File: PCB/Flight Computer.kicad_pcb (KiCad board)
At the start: 6 copper layers, 30 x 60 mm, 115 parts, among them J401 Conn_01x05_Pin, J402 USB_C_Receptacle_USB2.0_16P, J403 Screw_Terminal_01x06, J404 Screw_Terminal_01x04, J405 Conn_02x04_Counter_Clockwise, J406 Conn_02x03_Counter_Clockwise, J407 Conn_01x06_Pin, J408 Conn_01x04, J501 Conn_Coaxial, Q101 FDN306P, Q401 SL2302S, Q601 SL2302S, Q602 SL2302S, Q603 SL2302S, SW401 SW_Push, SW402 SW_Push, U101 LM1117MP-3.3, U201 STM32F446RETx, U202 W25Q128JVS, U301 SAM-M8Q, U302 LSM6DSV320, U303 MMC5633NJL, U304 MS5607-02BA, U501 SX1262IMLTRT, U502 SKY13453-385LF, Y201 Resonator, Y501 32 MHz

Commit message: Used KiCad's annotation tool to reannotate some of the parts Updated BOM
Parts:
- renumbered D406 to D403, D403 to D404, J407 to J403, J403 to J404, J404 to J405, J405 to J406, J406 to J407, R203 to R202, R202 to R203, R404 to R403, R406 to R404, R407 to R405, R408 to R406
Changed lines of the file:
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@@
 		(descr "2.0mm x 2.0mm Addressable RGB LED NeoPixel Nano, 12 mA, https://cdn-shop.adafruit.com/product-files/4684/4684_WS2812B-2020_V1.3_EN.pdf")
 		(tags "LED RGB NeoPixel Nano PLCC-4 2020")
-		(property "Reference" "D403"
+		(property "Reference" "D404"
 			(at 0 -2 0)
 			(layer "User.1")
@@
 		(descr "Through hole straight pin header, 1x06, 2.54mm pitch, single row")
 		(tags "Through hole pin header THT 1x06 2.54mm single row")
-		(property "Reference" "J407"
+		(property "Reference" "J403"
 			(at 0 -2.38 0)
 			(layer "F.Fab")
@@
 			)
 		)
-		(attr through_hole)
+		(attr through_hole exclude_from_pos_files exclude_from_bom)
 		(duplicate_pad_numbers_are_jumpers no)
 		(fp_line
@@
 		(descr "Resistor SMD 0603 (1608 Metric), square (rectangular) end terminal, IPC-7351 nominal with elongated pad for handsoldering. (Body size source: IPC-SM-782 page 72, https://www.pcb-3d.com/wordpress/wp-content/uploads/ipc-sm-782a_amendment_1_and_2.pdf), generated with kicad-footprint-generator")
 		(tags "resistor handsolder")
-		(property "Reference" "R404"
+		(property "Reference" "R403"
 			(at 0 -1.43 90)
 			(layer "User.1")
@@
 		(descr "Terminal Block Phoenix MPT-0,5-4-2.54, 4 pins, pitch 2.54mm, size 10.6x6.2mm, drill diameter 1.1mm, pad diameter 2.2mm, http://www.mouser.com/ds/2/324/ItemDetail_1725672-916605.pdf, script-generated using https://gitlab.com/kicad/libraries/kicad-footprint-generator/-/tree/master/scripts/TerminalBlock_Phoenix")
 		(tags "THT Terminal Block Phoenix MPT-0,5-4-2.54 pitch 2.54mm size 10.6x6.2mm drill 1.1mm pad 2.2mm")
-		(property "Reference" "J404"
+		(property "Reference" "J405"
 			(at -0.000001 1.97 90)
 			(layer "User.1")
@@
 		(layer "F.Cu")
 		(at 125.5 76.63 -90)
-		(property "Reference" "J405"
+		(property "Reference" "J406"
 			(at 2.032 2.54 270)
 			(unlocked yes)
@@
 			)
 		)
-		(attr smd)
+		(attr smd exclude_from_pos_files exclude_from_bom)
 		(duplicate_pad_numbers_are_jumpers no)
 		(fp_rect
@@
 		(descr "Terminal Block Phoenix MPT-0,5-6-2.54, 6 pins, pitch 2.54mm, size 15.7x6.2mm, drill diameter 1.1mm, pad diameter 2.2mm, http://www.mouser.com/ds/2/324/ItemDetail_1725672-916605.pdf, script-generated using https://gitlab.com/kicad/libraries/kicad-footprint-generator/-/tree/master/scripts/TerminalBlock_Phoenix")
 		(tags "THT Terminal Block Phoenix MPT-0,5-6-2.54 pitch 2.54mm size 15.7x6.2mm drill 1.1mm pad 2.2mm")
-		(property "Reference" "J403"
+		(property "Reference" "J404"
 			(at 0 2.05 90)
 			(layer "User.1")
@@
 		(descr "LED SMD 0603 (1608 Metric), square (rectangular) end terminal, IPC-7351 nominal, (Body size source: http://www.tortai-tech.com/upload/download/2011102023233369053.pdf), generated with kicad-footprint-generator")
 		(tags "LED handsolder")
-		(property "Reference" "D406"
+		(property "Reference" "D403"
 			(at 0 -1.43 90)
 			(layer "User.1")
@@
 			)
 		)
-		(attr through_hole)
+		(attr through_hole exclude_from_pos_files exclude_from_bom)
 		(duplicate_pad_numbers_are_jumpers no)
 		(fp_line
@@
 		(layer "F.Cu")
 		(at 115.47 54.35)
-		(property "Reference" "J406"
+		(property "Reference" "J407"
 			(at -1.17 0.006 90)
 			(unlocked yes)
@@
 			)
 		)
-		(attr smd exclude_from_bom)
+		(attr smd exclude_from_pos_files exclude_from_bom)
 		(duplicate_pad_numbers_are_jumpers no)
 		(fp_rect
@@
 		(descr "Resistor SMD 0603 (1608 Metric), square (rectangular) end terminal, IPC-7351 nominal with elongated pad for handsoldering. (Body size source: IPC-SM-782 page 72, https://www.pcb-3d.com/wordpress/wp-content/uploads/ipc-sm-782a_amendment_1_and_2.pdf), generated with kicad-footprint-generator")
 		(tags "resistor handsolder")
-		(property "Reference" "R406"
+		(property "Reference" "R404"
 			(at 0 1.43 90)
 			(layer "User.1")
@@
 		(descr "Resistor SMD 0603 (1608 Metric), square (rectangular) end terminal, IPC-7351 nominal with elongated pad for handsoldering. (Body size source: IPC-SM-782 page 72, https://www.pcb-3d.com/wordpress/wp-content/uploads/ipc-sm-782a_amendment_1_and_2.pdf), generated with kicad-footprint-generator")
 		(tags "resistor handsolder")
-		(property "Reference" "R407"
+		(property "Reference" "R405"
 			(at 0 1.43 0)
 			(layer "User.2")
@@
 		(descr "Resistor SMD 0603 (1608 Metric), square (rectangular) end terminal, IPC-7351 nominal with elongated pad for handsoldering. (Body size source: IPC-SM-782 page 72, https://www.pcb-3d.com/wordpress/wp-content/uploads/ipc-sm-782a_amendment_1_and_2.pdf), generated with kicad-footprint-generator")
 		(tags "resistor handsolder")
-		(property "Reference" "R202"
+		(property "Reference" "R203"
 			(at 0 1.43 0)
 			(layer "User.2")
@@
 		(descr "Resistor SMD 0603 (1608 Metric), square (rectangular) end terminal, IPC-7351 nominal with elongated pad for handsoldering. (Body size source: IPC-SM-782 page 72, https://www.pcb-3d.com/wordpress/wp-content/uploads/ipc-sm-782a_amendment_1_and_2.pdf), generated with kicad-footprint-generator")
 		(tags "resistor handsolder")
-		(property "Reference" "R408"
+		(property "Reference" "R406"
 			(at 0 1.43 90)
 			(layer "User.2")
@@
 		(descr "Resistor SMD 0603 (1608 Metric), square (rectangular) end terminal, IPC-7351 nominal with elongated pad for handsoldering. (Body size source: IPC-SM-782 page 72, https://www.pcb-3d.com/wordpress/wp-content/uploads/ipc-sm-782a_amendment_1_and_2.pdf), generated with kicad-footprint-generator")
 		(tags "resistor handsolder")
-		(property "Reference" "R203"
+		(property "Reference" "R202"
 			(at 0 1.43 90)
 			(layer "User.2")

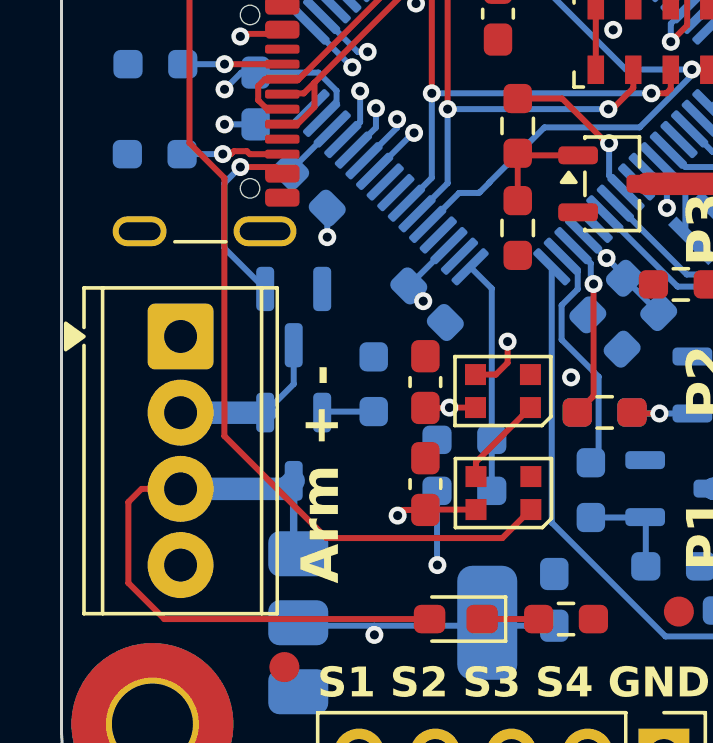
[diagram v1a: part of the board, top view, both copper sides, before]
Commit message: Made it so USB isn't putting 4.7v into the battery
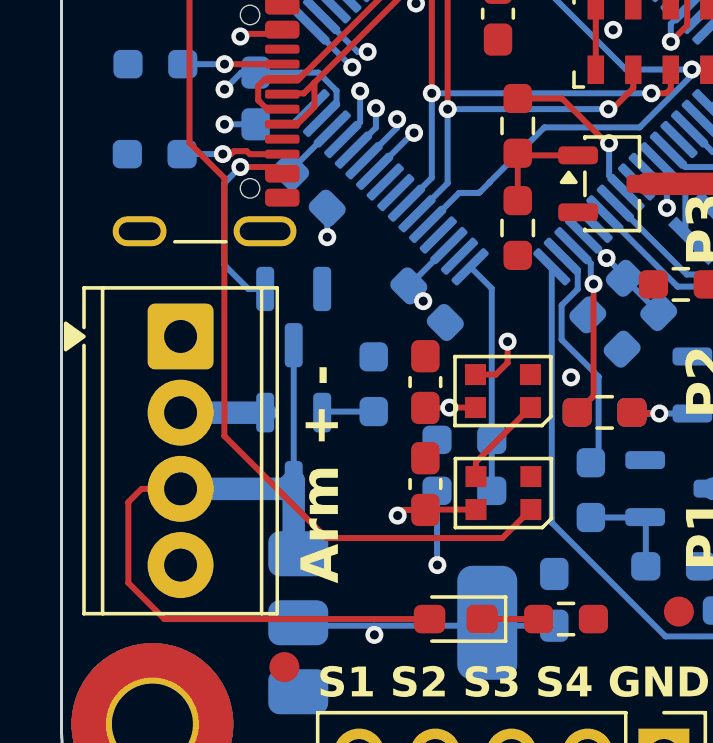
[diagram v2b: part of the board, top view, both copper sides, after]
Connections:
- D401 pad 3: VBAT -> VCC
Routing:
- net VCC: track 21.6 -> 26.2 mm
- net VBAT: track 42.8 -> 40.1 mm
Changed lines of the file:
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@@
 			(layers "B.Cu" "B.Mask" "B.Paste")
 			(roundrect_rratio 0.25)
-			(net "VBAT")
+			(net "VCC")
 			(pinfunction "K_3")
 			(pintype "passive")
@@
 	)
 	(segment
-		(start 105.41 98.1663)
-		(end 104.46 99.1163)
-		(width 0.2)
-		(layer "B.Cu")
-		(net "VBAT")
-	)
-	(segment
-		(start 105.41 96.871)
-		(end 105.41 98.1663)
-		(width 0.2)
-		(layer "B.Cu")
-		(net "VBAT")
-	)
-	(segment
 		(start 101.64 99.12)
 		(end 104.4563 99.12)
@@
 		(start 105.41 103.7708)
 		(end 105.41 101.3913)
-		(width 0.25)
+		(width 0.75)
 		(layer "B.Cu")
 		(net "VCC")
@@
 	)
 	(segment
+		(start 105.41 96.871)
+		(end 105.41 101.3913)
+		(width 0.2)
+		(layer "B.Cu")
+		(net "VCC")
+	)
+	(segment
 		(start 105.41 101.3913)
 		(end 105.141301 101.659999)
@@
 	)
 	(segment
-		(start 103.1 93.636)
-		(end 104.46 94.996)
+		(start 103.1 94.2)
+		(end 103.896 94.996)
 		(width 0.2)
 		(layer "B.Cu")
@@
 	(segment
 		(start 103.1 91.464)
-		(end 103.1 93.636)
+		(end 103.1 94.2)
+		(width 0.2)
+		(layer "B.Cu")
+		(net "VBUS")
+	)
+	(segment
+		(start 103.896 94.996)
+		(end 104.46 94.996)
 		(width 0.2)
 		(layer "B.Cu")

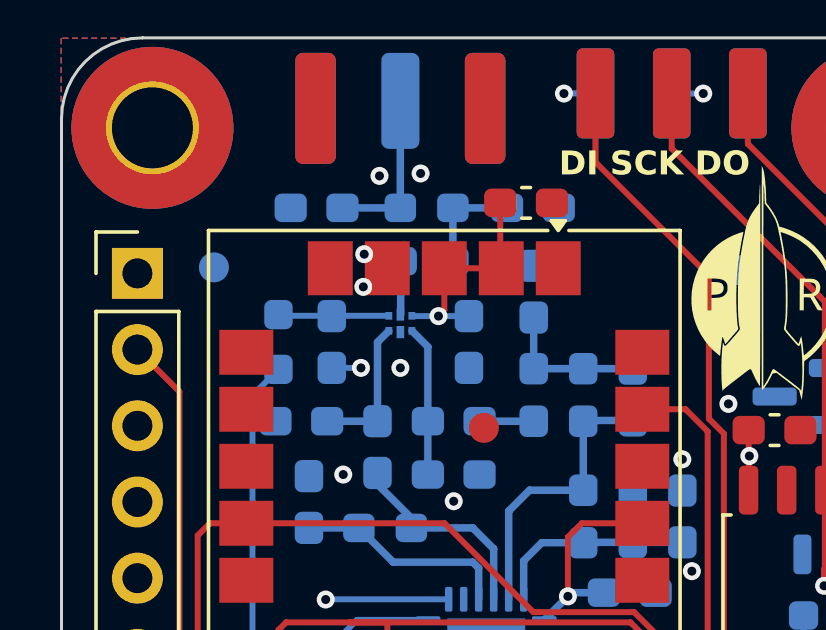
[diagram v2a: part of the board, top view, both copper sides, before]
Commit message: Create github action to run kicad jobset and push the output files
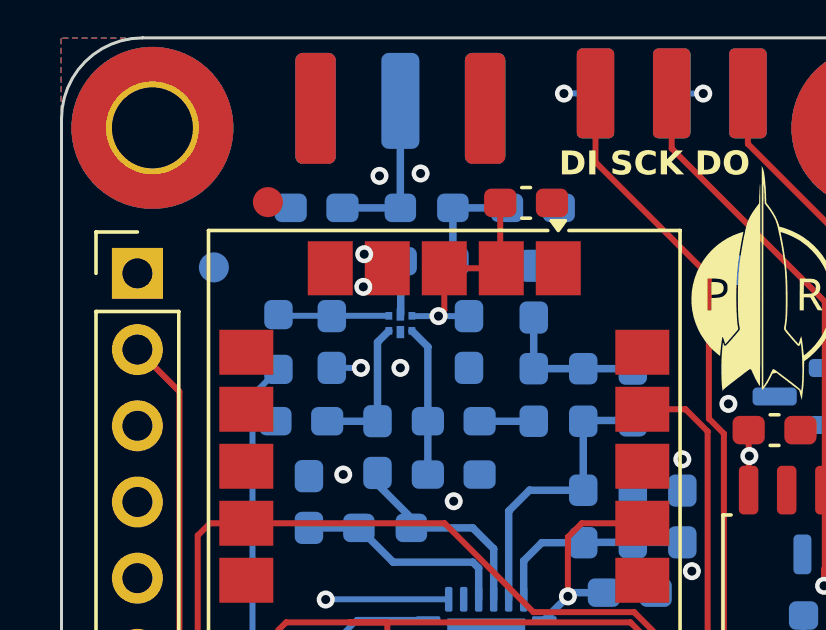
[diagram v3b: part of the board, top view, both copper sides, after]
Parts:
- moved FID405 10.4 mm to (104.5, 58.0)
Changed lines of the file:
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@@
 	(footprint "Fiducial:Fiducial_1mm_Mask2mm"
 		(layer "F.Cu")
-		(at 111.75 65.5)
+		(at 104.55 57.975)
 		(descr "Fiducial, circular marking, 1mm bare copper, 2mm soldermask opening (Level A)")
 		(tags "fiducial")
@@
 			)
 		)
+		(property "KiLib_Generator" "fiducial"
+			(at 0 0 0)
+			(layer "F.SilkS")
+			(hide yes)
+			(effects
+				(font
+					(size 1 1)
+					(thickness 0.15)
+				)
+			)
+		)
 		(property ki_fp_filters "Fiducial*")
 		(sheetname "/IO/")
 		(sheetfile "IO.kicad_sch")
-		(units
-			(unit
-				(name "A")
-				(pins)
-			)
-		)
 		(attr smd exclude_from_bom)
 		(duplicate_pad_numbers_are_jumpers no)
 		(fp_circle
 			(center 0 0)
+			(end 0.635 0)
+			(stroke
+				(width 0.05)
+				(type solid)
+			)
+			(fill no)
+			(layer "F.CrtYd")
+		)
+		(fp_circle
+			(center 0 0)

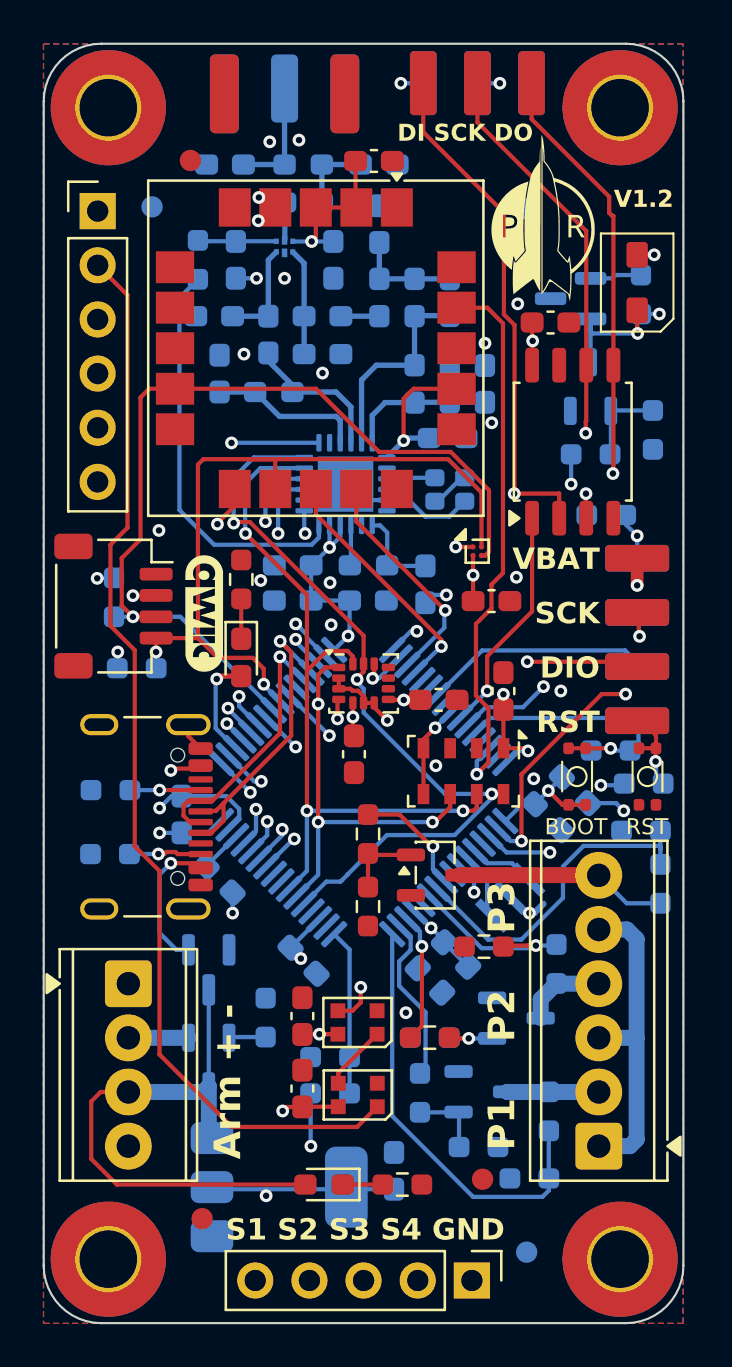
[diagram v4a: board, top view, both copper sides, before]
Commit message: Added VCC to the servo header
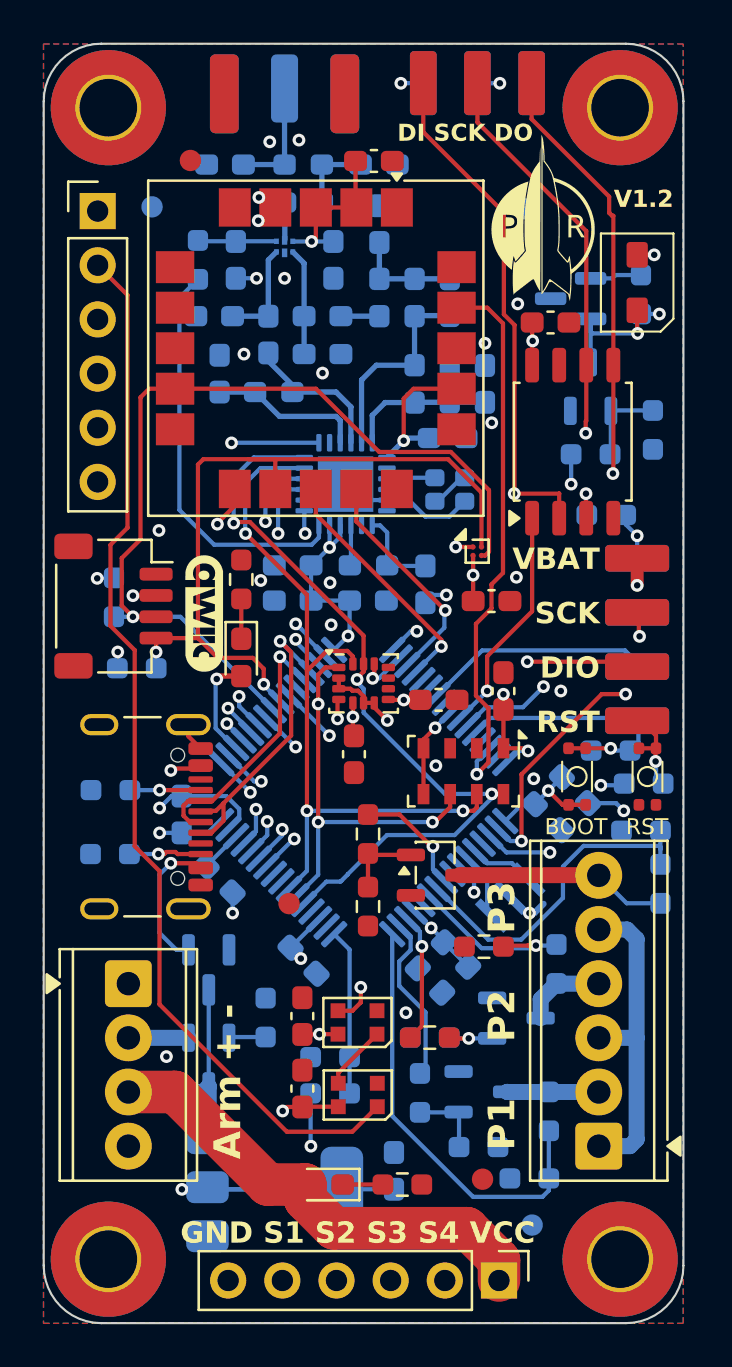
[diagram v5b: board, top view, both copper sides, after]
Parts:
- J401: footprint Connector_PinHeader_2.54mm:PinHeader_1x05_P2.54mm_Vertical -> Connector_PinHeader_2.54mm:PinHeader_1x06_P2.54mm_Vertical
- moved FID406 15.3 mm to (109.2, 92.8)
- moved FID403 1.30 mm to (120.6, 107.9)
- moved J401 1.27 mm to (119.0, 110.5)
- moved U101 0.21 mm to (108.5, 106.1)
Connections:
- J401 pad 1: GND -> VCC
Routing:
- net VCC: track 26.2 -> 33.0 mm
- net +3.3V: track 72.1 -> 75.8 mm
- net /IO/NEOPIXEL_DO: track 50.9 -> 49.7 mm
- net /PB1: track 24.6 -> 25.2 mm
- net /PB10: track 24.0 -> 24.5 mm
- net /PB2: track 24.1 -> 24.6 mm
- net /PB0: track 25.0 -> 25.5 mm
- net GND: vias 29 -> 30
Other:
- board text added: "GND S1 S2 S3 S4 VCC"
- board text removed: "S1 S2 S3 S4 GND"

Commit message: swapped power and gnd on the servo header
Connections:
- J401 pad 1: VCC -> GND
- J401 pad 6: GND -> VCC
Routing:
- net VCC: track 33.0 -> 25.7 mm
- net GND: vias 30 -> 31
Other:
- board text added: "VCC S1 S2 S3 S4 GND"
- board text removed: "GND S1 S2 S3 S4 VCC"
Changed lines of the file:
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@@
 			(layers "*.Cu" "*.Mask")
 			(remove_unused_layers no)
-			(net "VCC")
+			(net "GND")
 			(pinfunction "Pin_1_1")
 			(pintype "passive")
@@
 			(layers "*.Cu" "*.Mask")
 			(remove_unused_layers no)
-			(net "GND")
+			(net "VCC")
 			(pinfunction "Pin_6_6")
 			(pintype "passive")
@@
 		)
 	)
-	(gr_text "GND S1 S2 S3 S4 VCC"
+	(gr_text "VCC S1 S2 S3 S4 GND"
 		(at 104.075 108.85 0)
 		(layer "F.SilkS" knockout)
@@
 		(layer "Dwgs.User")
 		(pts
-			(xy 104.23 52.5) (xy 102.21 112.5)
+			(xy 103.755 50.828) (xy 101.735 110.828)
 		)
 		(height -12.98)
@@
 		)
 		(gr_text "60"
-			(at 90.1 82.5 90)
+			(at 89.625 80.828 90)
 			(layer "Dwgs.User")
 			(effects
@@
 	)
 	(via
+		(at 108.025 106.925)
+		(size 0.6)
+		(drill 0.3)
+		(layers "F.Cu" "B.Cu")
+		(free yes)
+		(net "GND")
+	)
+	(via
 		(at 103.075 75.325)
 		(size 0.6)
@@
 	)
 	(via
-		(at 103.425 100)
+		(at 103.8 107.15)
 		(size 0.6)
 		(drill 0.3)
@@
 	)
 	(segment
+		(start 108.877354 102.372646)
+		(end 109.052354 102.372646)
+		(width 0.2)
+		(layer "F.Cu")
+		(net "+3.3V")
+	)
+	(segment
 		(start 115.0128 68.68)
 		(end 114.55 69.1428)
@@
 	)
 	(segment
-		(start 109.0625 102.3625)
-		(end 109.8 102.3625)
-		(width 0.2)
-		(layer "F.Cu")
-		(net "+3.3V")
-	)
-	(segment
-		(start 108.875 102.55)
-		(end 109.0625 102.3625)
-		(width 0.2)
-		(layer "F.Cu")
-		(net "+3.3V")
-	)
-	(segment
 		(start 112.17 84.907499)
 		(end 112.22 84.957499)
@@
 	)
 	(segment
+		(start 109.0625 102.3625)
+		(end 109.8 102.3625)
+		(width 0.2)
+		(layer "F.Cu")
+		(net "+3.3V")
+	)
+	(segment
 		(start 110.43 61.581)
 		(end 110.236 61.775)
@@
 	)
 	(segment
+		(start 109.052354 102.372646)
+		(end 109.0625 102.3625)
+		(width 0.2)
+		(layer "F.Cu")
+		(net "+3.3V")
+	)
+	(segment
 		(start 120.5992 67.4072)
 		(end 120.576 67.384)
@@
 	)
 	(via
-		(at 108.875 102.55)
+		(at 108.877354 102.372646)
 		(size 0.6)
 		(drill 0.3)
@@
 	)
 	(segment
-		(start 101.6 75.2)
-		(end 101.6 64.29)
+		(start 100.8 76)
+		(end 101.6 75.2)
 		(width 0.2)
 		(layer "F.Cu")
@@
 	)
 	(segment
-		(start 101.938 90.135805)
-		(end 101.938 80.938)
+		(start 103.1 91.297805)
+		(end 101.938 90.135805)
 		(width 0.2)
 		(layer "F.Cu")
@@
 	)
 	(segment
-		(start 112.14 103.525)
-		(end 109.075 103.525)
+		(start 103.1 97.6)
+		(end 103.1 91.297805)
 		(width 0.2)
 		(layer "F.Cu")
@@
 	(segment
 		(start 113.315 102.35)
-		(end 112.14 103.525)
+		(end 112.39 103.275)
 		(width 0.2)
 		(layer "F.Cu")
@@
 	)
 	(segment
-		(start 100.8 79.8)
-		(end 100.8 76)
+		(start 101.6 64.29)
+		(end 100.2 62.89)
 		(width 0.2)
 		(layer "F.Cu")
@@
 	)
 	(segment
-		(start 103.1 91.297805)
-		(end 101.938 90.135805)
+		(start 100.8 79.8)
+		(end 100.8 76)
 		(width 0.2)
 		(layer "F.Cu")
@@
 	)
 	(segment
-		(start 100.8 76)
-		(end 101.6 75.2)
+		(start 101.938 90.135805)
+		(end 101.938 80.938)
 		(width 0.2)
 		(layer "F.Cu")
@@
 	)
 	(segment
-		(start 109.075 103.525)
-		(end 103.1 97.55)
+		(start 101.6 75.2)
+		(end 101.6 64.29)
 		(width 0.2)
 		(layer "F.Cu")
@@
 	)
 	(segment
-		(start 101.6 64.29)
-		(end 100.2 62.89)
+		(start 101.938 80.938)
+		(end 100.8 79.8)
 		(width 0.2)
 		(layer "F.Cu")
@@
 	)
 	(segment
-		(start 101.938 80.938)
-		(end 100.8 79.8)
+		(start 112.39 103.275)
+		(end 108.775 103.275)
 		(width 0.2)
 		(layer "F.Cu")
@@
 	)
 	(segment
-		(start 103.1 97.55)
-		(end 103.1 91.297805)
+		(start 108.775 103.275)
+		(end 103.1 97.6)
 		(width 0.2)
 		(layer "F.Cu")
@@
 	(segment
 		(start 109.939302 106)
-		(end 109.939302 106.711276)
-		(width 2)
-		(layer "F.Cu")
-		(net "VCC")
-	)
-	(segment
-		(start 108.175 106)
-		(end 109.939302 106)
-		(width 2)
+		(end 106.898 106)
+		(width 0.2)
 		(layer "F.Cu")
 		(net "VCC")
 	)
 	(segment
-		(start 103.834999 101.659999)
-		(end 108.175 106)
-		(width 2)
+		(start 106.298 104.762365)
+		(end 106.298 106.6)
+		(width 2.6)
 		(layer "F.Cu")
 		(net "VCC")
 	)
 	(segment
-		(start 111.278026 108.05)
-		(end 117.525 108.05)
-		(width 2)
+		(start 106.298 106.6)
+		(end 106.298 110.478048)
+		(width 2.6)
 		(layer "F.Cu")
 		(net "VCC")
 	)
 	(segment
-		(start 109.939302 106.711276)
-		(end 111.278026 108.05)
-		(width 2)
+		(start 103.195634 101.659999)
+		(end 106.298 104.762365)
+		(width 2.6)
 		(layer "F.Cu")
 		(net "VCC")
@@
 	(segment
 		(start 101.64 101.659999)
-		(end 103.834999 101.659999)
-		(width 2)
-		(layer "F.Cu")
-		(net "VCC")
-	)
-	(segment
-		(start 117.525 108.05)
-		(end 119.019952 109.544952)
-		(width 2)
+		(end 103.195634 101.659999)
+		(width 2.6)
 		(layer "F.Cu")
 		(net "VCC")
 	)
 	(segment
-		(start 119.019952 109.544952)
-		(end 119.019952 110.5)
-		(width 2)
+		(start 106.298 110.478048)
+		(end 106.319952 110.5)
+		(width 2.6)
 		(layer "F.Cu")
 		(net "VCC")
